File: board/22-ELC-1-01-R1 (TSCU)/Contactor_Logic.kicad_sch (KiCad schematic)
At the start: 16 parts, among them U2 74AUC1G17, U5 LM393, U6 74HC08_2AND

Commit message: Ready for review
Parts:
- removed R40, R44: 500, symbol Device:R
- removed unit 2 of U5
- renumbered C13 to C10, C11 to C8, C12 to C9, R23 to R15, R24 to R16, R25 to R19, TP5 to TP10, TP6 to TP11, TP18 to TP12, TP7 to TP13, U2 to U3, U5 to U4, U6 to U5

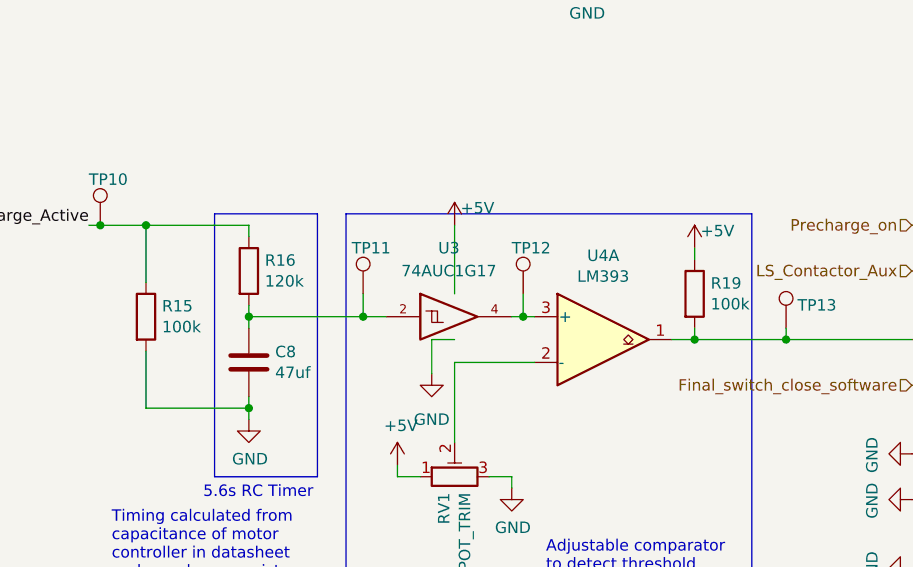
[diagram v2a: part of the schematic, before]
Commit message: All good except need to switch everything to accepting 24v power
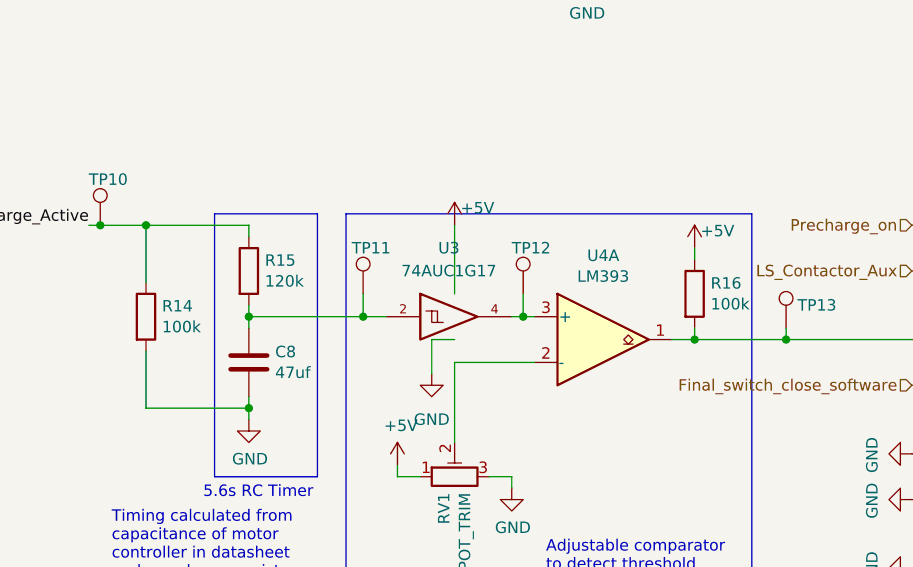
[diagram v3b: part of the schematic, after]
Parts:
- U3: footprint (none) -> Package_TO_SOT_SMD:SOT-23-5
- renumbered R15 to R14, R16 to R15, R19 to R16
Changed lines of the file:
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@@
   (symbol (lib_id "power:+5V") (at 119.38 130.81 0) (unit 1)
     (in_bom yes) (on_board yes)
-    (property "Reference" "#PWR038" (id 0) (at 119.38 134.62 0)
+    (property "Reference" "#PWR039" (id 0) (at 119.38 134.62 0)
       (effects (font (size 1.27 1.27)) hide)
     )
@@
   (symbol (lib_id "power:GND") (at 132.08 133.35 0) (unit 1)
     (in_bom yes) (on_board yes)
-    (property "Reference" "#PWR041" (id 0) (at 132.08 139.7 0)
+    (property "Reference" "#PWR042" (id 0) (at 132.08 139.7 0)
       (effects (font (size 1.27 1.27)) hide)
     )
@@
   (symbol (lib_id "Device:R") (at 102.87 109.22 0) (unit 1)
     (in_bom yes) (on_board yes)
-    (property "Reference" "R16" (id 0) (at 104.648 108.0516 0)
+    (property "Reference" "R15" (id 0) (at 104.648 108.0516 0)
       (effects (font (size 1.27 1.27)) (justify left))
     )
@@
   (symbol (lib_id "power:GND") (at 102.87 125.73 0) (unit 1)
     (in_bom yes) (on_board yes)
-    (property "Reference" "#PWR037" (id 0) (at 102.87 132.08 0)
+    (property "Reference" "#PWR038" (id 0) (at 102.87 132.08 0)
       (effects (font (size 1.27 1.27)) hide)
     )
@@
   (symbol (lib_id "Device:R") (at 91.44 114.3 0) (unit 1)
     (in_bom yes) (on_board yes)
-    (property "Reference" "R15" (id 0) (at 93.218 113.1316 0)
+    (property "Reference" "R14" (id 0) (at 93.218 113.1316 0)
       (effects (font (size 1.27 1.27)) (justify left))
     )
@@
   (symbol (lib_id "Device:R") (at 152.4 111.76 0) (unit 1)
     (in_bom yes) (on_board yes)
-    (property "Reference" "R19" (id 0) (at 154.178 110.5916 0)
+    (property "Reference" "R16" (id 0) (at 154.178 110.5916 0)
       (effects (font (size 1.27 1.27)) (justify left))
     )
@@
     (property "Reference" "U3" (id 0) (at 125.095 106.68 0))
     (property "Value" "74AUC1G17" (id 1) (at 125.095 109.22 0))
-    (property "Footprint" "" (id 2) (at 125.73 114.3 0)
+    (property "Footprint" "Package_TO_SOT_SMD:SOT-23-5" (id 2) (at 125.73 114.3 0)
       (effects (font (size 1.27 1.27)) hide)
     )
@@
   (symbol (lib_id "power:+5V") (at 125.73 104.14 0) (unit 1)
     (in_bom yes) (on_board yes)
-    (property "Reference" "#PWR040" (id 0) (at 125.73 107.95 0)
+    (property "Reference" "#PWR041" (id 0) (at 125.73 107.95 0)
       (effects (font (size 1.27 1.27)) hide)
     )
@@
   (symbol (lib_id "power:GND") (at 123.19 120.65 0) (unit 1)
     (in_bom yes) (on_board yes) (fields_autoplaced)
-    (property "Reference" "#PWR039" (id 0) (at 123.19 127 0)
-      (effects (font (size 1.27 1.27)) hide)
-    )
+    (property "Reference" "#PWR040" (id 0) (at 123.19 127 0)
+      (effects (font (size 1.27 1.27)) hide)
+    )

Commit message: Finalized schematic, started board layout
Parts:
- C10, C9: footprint Capacitor_SMD:C_0603_1608Metric_Pad1.08x0.95mm_HandSolder -> Capacitor_SMD:C_0402_1005Metric
- C8: footprint Capacitor_SMD:C_1206_3216Metric_Pad1.33x1.80mm_HandSolder -> Capacitor_SMD:C_0402_1005Metric
- R14, R15, R16: footprint Resistor_SMD:R_0603_1608Metric_Pad0.98x0.95mm_HandSolder -> FixedTextSizes:R_0402_1005Metric
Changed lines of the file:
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@@
   (symbol (lib_id "power:+5V") (at 119.38 130.81 0) (unit 1)
     (in_bom yes) (on_board yes)
-    (property "Reference" "#PWR039" (id 0) (at 119.38 134.62 0)
+    (property "Reference" "#PWR038" (id 0) (at 119.38 134.62 0)
       (effects (font (size 1.27 1.27)) hide)
     )
@@
   (symbol (lib_id "power:GND") (at 132.08 133.35 0) (unit 1)
     (in_bom yes) (on_board yes)
-    (property "Reference" "#PWR042" (id 0) (at 132.08 139.7 0)
+    (property "Reference" "#PWR041" (id 0) (at 132.08 139.7 0)
       (effects (font (size 1.27 1.27)) hide)
     )
@@
       (effects (font (size 1.27 1.27)) (justify left))
     )
-    (property "Footprint" "Resistor_SMD:R_0603_1608Metric_Pad0.98x0.95mm_HandSolder" (id 2) (at 101.092 109.22 90)
+    (property "Footprint" "FixedTextSizes:R_0402_1005Metric" (id 2) (at 101.092 109.22 90)
       (effects (font (size 1.27 1.27)) hide)
     )
@@
       (effects (font (size 1.27 1.27)) (justify left))
     )
-    (property "Footprint" "Capacitor_SMD:C_1206_3216Metric_Pad1.33x1.80mm_HandSolder" (id 2) (at 103.8352 123.19 0)
+    (property "Footprint" "Capacitor_SMD:C_0402_1005Metric" (id 2) (at 103.8352 123.19 0)
       (effects (font (size 1.27 1.27)) hide)
     )
@@
   (symbol (lib_id "power:GND") (at 102.87 125.73 0) (unit 1)
     (in_bom yes) (on_board yes)
-    (property "Reference" "#PWR038" (id 0) (at 102.87 132.08 0)
+    (property "Reference" "#PWR037" (id 0) (at 102.87 132.08 0)
       (effects (font (size 1.27 1.27)) hide)
     )
@@
       (effects (font (size 1.27 1.27)) (justify left))
     )
-    (property "Footprint" "Resistor_SMD:R_0603_1608Metric_Pad0.98x0.95mm_HandSolder" (id 2) (at 89.662 114.3 90)
+    (property "Footprint" "FixedTextSizes:R_0402_1005Metric" (id 2) (at 89.662 114.3 90)
       (effects (font (size 1.27 1.27)) hide)
     )
@@
   (symbol (lib_id "power:+5V") (at 187.96 83.82 0) (unit 1)
     (in_bom yes) (on_board yes)
-    (property "Reference" "#PWR051" (id 0) (at 187.96 87.63 0)
+    (property "Reference" "#PWR050" (id 0) (at 187.96 87.63 0)
       (effects (font (size 1.27 1.27)) hide)
     )
@@
     (property "Reference" "C10" (id 0) (at 193.04 81.8134 90))
     (property "Value" "0.1uf" (id 1) (at 193.04 84.1248 90))
-    (property "Footprint" "Capacitor_SMD:C_0603_1608Metric_Pad1.08x0.95mm_HandSolder" (id 2) (at 193.04 87.63 0)
+    (property "Footprint" "Capacitor_SMD:C_0402_1005Metric" (id 2) (at 193.04 87.63 0)
       (effects (font (size 1.27 1.27)) hide)
     )
@@
   (symbol (lib_id "power:GND") (at 187.96 151.13 0) (unit 1)
     (in_bom yes) (on_board yes)
-    (property "Reference" "#PWR052" (id 0) (at 187.96 157.48 0)
+    (property "Reference" "#PWR051" (id 0) (at 187.96 157.48 0)
       (effects (font (size 1.27 1.27)) hide)
     )
@@
   (symbol (lib_id "power:GND") (at 196.85 88.9 0) (unit 1)
     (in_bom yes) (on_board yes)
-    (property "Reference" "#PWR053" (id 0) (at 196.85 95.25 0)
+    (property "Reference" "#PWR052" (id 0) (at 196.85 95.25 0)
       (effects (font (size 1.27 1.27)) hide)
     )
@@
   (symbol (lib_id "power:+5V") (at 140.335 54.61 0) (unit 1)
     (in_bom yes) (on_board yes)
-    (property "Reference" "#PWR043" (id 0) (at 140.335 58.42 0)
+    (property "Reference" "#PWR042" (id 0) (at 140.335 58.42 0)
       (effects (font (size 1.27 1.27)) hide)
     )
@@
   (symbol (lib_id "power:GND") (at 140.335 76.2 0) (unit 1)
     (in_bom yes) (on_board yes)
-    (property "Reference" "#PWR044" (id 0) (at 140.335 82.55 0)
+    (property "Reference" "#PWR043" (id 0) (at 140.335 82.55 0)
       (effects (font (size 1.27 1.27)) hide)
     )
@@
     (property "Reference" "C9" (id 0) (at 146.685 51.3334 90))
     (property "Value" "0.1uf" (id 1) (at 146.685 53.6448 90))
-    (property "Footprint" "Capacitor_SMD:C_0603_1608Metric_Pad1.08x0.95mm_HandSolder" (id 2) (at 146.685 57.15 0)
+    (property "Footprint" "Capacitor_SMD:C_0402_1005Metric" (id 2) (at 146.685 57.15 0)
       (effects (font (size 1.27 1.27)) hide)
     )
@@
   (symbol (lib_id "power:GND") (at 150.495 58.42 0) (unit 1)
     (in_bom yes) (on_board yes)
-    (property "Reference" "#PWR045" (id 0) (at 150.495 64.77 0)
+    (property "Reference" "#PWR044" (id 0) (at 150.495 64.77 0)
       (effects (font (size 1.27 1.27)) hide)
     )
@@
       (effects (font (size 1.27 1.27)) (justify left))
     )
-    (property "Footprint" "Resistor_SMD:R_0603_1608Metric_Pad0.98x0.95mm_HandSolder" (id 2) (at 150.622 111.76 90)
+    (property "Footprint" "FixedTextSizes:R_0402_1005Metric" (id 2) (at 150.622 111.76 90)
       (effects (font (size 1.27 1.27)) hide)
     )
@@
   (symbol (lib_id "power:+5V") (at 152.4 106.68 0) (unit 1)
     (in_bom yes) (on_board yes)
-    (property "Reference" "#PWR046" (id 0) (at 152.4 110.49 0)
+    (property "Reference" "#PWR045" (id 0) (at 152.4 110.49 0)
       (effects (font (size 1.27 1.27)) hide)
     )
@@
   (symbol (lib_id "power:GND") (at 176.53 129.54 270) (unit 1)
     (in_bom yes) (on_board yes)
-    (property "Reference" "#PWR047" (id 0) (at 170.18 129.54 0)
+    (property "Reference" "#PWR046" (id 0) (at 170.18 129.54 0)
       (effects (font (size 1.27 1.27)) hide)
     )
@@
   (symbol (lib_id "power:GND") (at 176.53 134.62 270) (unit 1)
     (in_bom yes) (on_board yes)
-    (property "Reference" "#PWR048" (id 0) (at 170.18 134.62 0)
+    (property "Reference" "#PWR047" (id 0) (at 170.18 134.62 0)
       (effects (font (size 1.27 1.27)) hide)
     )
@@
   (symbol (lib_id "power:GND") (at 176.53 142.24 270) (unit 1)
     (in_bom yes) (on_board yes)
-    (property "Reference" "#PWR049" (id 0) (at 170.18 142.24 0)
+    (property "Reference" "#PWR048" (id 0) (at 170.18 142.24 0)
       (effects (font (size 1.27 1.27)) hide)
     )
@@
   (symbol (lib_id "power:GND") (at 176.53 147.32 270) (unit 1)
     (in_bom yes) (on_board yes)
-    (property "Reference" "#PWR050" (id 0) (at 170.18 147.32 0)
+    (property "Reference" "#PWR049" (id 0) (at 170.18 147.32 0)
       (effects (font (size 1.27 1.27)) hide)
     )
@@
   (symbol (lib_id "power:+5V") (at 125.73 104.14 0) (unit 1)
     (in_bom yes) (on_board yes)
-    (property "Reference" "#PWR041" (id 0) (at 125.73 107.95 0)
+    (property "Reference" "#PWR040" (id 0) (at 125.73 107.95 0)
       (effects (font (size 1.27 1.27)) hide)
     )
@@
   (symbol (lib_id "power:GND") (at 123.19 120.65 0) (unit 1)
     (in_bom yes) (on_board yes) (fields_autoplaced)
-    (property "Reference" "#PWR040" (id 0) (at 123.19 127 0)
-      (effects (font (size 1.27 1.27)) hide)
-    )
+    (property "Reference" "#PWR039" (id 0) (at 123.19 127 0)
+      (effects (font (size 1.27 1.27)) hide)
+    )

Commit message: More progress
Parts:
- C10, C8, C9: footprint Capacitor_SMD:C_0402_1005Metric -> FixedTextSizes:C_0402_1005Metric_Pad0.74x0.62mm_HandSolder_Reasonable_Text_Size
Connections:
- net Precharge_Timer_Out: now reaches C8.1, R15.2, TP11.1, U3.2
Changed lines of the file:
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@@
 (kicad_sch (version 20211123) (generator eeschema)
   (paper "A4")
+  (junction (at 111.76 114.3) (diameter 0) (color 0 0 0 0)
+  )
   (junction (at 152.4 116.84) (diameter 0) (color 0 0 0 0)
   )
@@
     (stroke (width 0) (type default) (color 0 0 0 0))
   )
-  (wire (pts (xy 102.87 114.3) (xy 115.57 114.3))
+  (wire (pts (xy 102.87 114.3) (xy 111.76 114.3))
     (stroke (width 0) (type default) (color 0 0 0 0))
   )
@@
     (stroke (width 0) (type default) (color 0 0 0 0))
   )
+  (wire (pts (xy 113.03 96.52) (xy 111.76 96.52))
+    (stroke (width 0) (type default) (color 0 0 0 0))
+  )
   (wire (pts (xy 133.35 111.76) (xy 133.35 114.3))
     (stroke (width 0) (type default) (color 0 0 0 0))
@@
     (stroke (width 0) (type default) (color 0 0 0 0))
   )
+  (wire (pts (xy 111.76 114.3) (xy 115.57 114.3))
+    (stroke (width 0) (type default) (color 0 0 0 0))
+  )
   (polyline (pts (xy 99.06 132.08) (xy 99.06 102.87))
     (stroke (width 0) (type default) (color 0 0 0 0))
@@
   )
   (wire (pts (xy 115.57 111.76) (xy 115.57 114.3))
+    (stroke (width 0) (type default) (color 0 0 0 0))
+  )
+  (wire (pts (xy 111.76 96.52) (xy 111.76 114.3))
     (stroke (width 0) (type default) (color 0 0 0 0))
   )
@@
     (effects (font (size 1.27 1.27)) (justify right))
   )
+  (hierarchical_label "Precharge_Timer_Out" (shape output) (at 113.03 96.52 0)
+    (effects (font (size 1.27 1.27)) (justify left))
+  )
   (hierarchical_label "Precharge_done" (shape output) (at 205.74 119.38 0)
     (effects (font (size 1.27 1.27)) (justify left))
@@
   (symbol (lib_id "power:+5V") (at 119.38 130.81 0) (unit 1)
     (in_bom yes) (on_board yes)
-    (property "Reference" "#PWR038" (id 0) (at 119.38 134.62 0)
+    (property "Reference" "#PWR041" (id 0) (at 119.38 134.62 0)
       (effects (font (size 1.27 1.27)) hide)
     )
@@
   (symbol (lib_id "power:GND") (at 132.08 133.35 0) (unit 1)
     (in_bom yes) (on_board yes)
-    (property "Reference" "#PWR041" (id 0) (at 132.08 139.7 0)
+    (property "Reference" "#PWR044" (id 0) (at 132.08 139.7 0)
       (effects (font (size 1.27 1.27)) hide)
     )
@@
       (effects (font (size 1.27 1.27)) (justify left))
     )
-    (property "Footprint" "Capacitor_SMD:C_0402_1005Metric" (id 2) (at 103.8352 123.19 0)
+    (property "Footprint" "FixedTextSizes:C_0402_1005Metric_Pad0.74x0.62mm_HandSolder_Reasonable_Text_Size" (id 2) (at 103.8352 123.19 0)
       (effects (font (size 1.27 1.27)) hide)
     )
@@
   (symbol (lib_id "power:GND") (at 102.87 125.73 0) (unit 1)
     (in_bom yes) (on_board yes)
-    (property "Reference" "#PWR037" (id 0) (at 102.87 132.08 0)
+    (property "Reference" "#PWR040" (id 0) (at 102.87 132.08 0)
       (effects (font (size 1.27 1.27)) hide)
     )
@@
   (symbol (lib_id "power:+5V") (at 187.96 83.82 0) (unit 1)
     (in_bom yes) (on_board yes)
-    (property "Reference" "#PWR050" (id 0) (at 187.96 87.63 0)
+    (property "Reference" "#PWR053" (id 0) (at 187.96 87.63 0)
       (effects (font (size 1.27 1.27)) hide)
     )
@@
     (property "Reference" "C10" (id 0) (at 193.04 81.8134 90))
     (property "Value" "0.1uf" (id 1) (at 193.04 84.1248 90))
-    (property "Footprint" "Capacitor_SMD:C_0402_1005Metric" (id 2) (at 193.04 87.63 0)
+    (property "Footprint" "FixedTextSizes:C_0402_1005Metric_Pad0.74x0.62mm_HandSolder_Reasonable_Text_Size" (id 2) (at 193.04 87.63 0)
       (effects (font (size 1.27 1.27)) hide)
     )
@@
   (symbol (lib_id "power:GND") (at 187.96 151.13 0) (unit 1)
     (in_bom yes) (on_board yes)
-    (property "Reference" "#PWR051" (id 0) (at 187.96 157.48 0)
+    (property "Reference" "#PWR054" (id 0) (at 187.96 157.48 0)
       (effects (font (size 1.27 1.27)) hide)
     )
@@
   (symbol (lib_id "power:GND") (at 196.85 88.9 0) (unit 1)
     (in_bom yes) (on_board yes)
-    (property "Reference" "#PWR052" (id 0) (at 196.85 95.25 0)
+    (property "Reference" "#PWR055" (id 0) (at 196.85 95.25 0)
       (effects (font (size 1.27 1.27)) hide)
     )
@@
   (symbol (lib_id "power:+5V") (at 140.335 54.61 0) (unit 1)
     (in_bom yes) (on_board yes)
-    (property "Reference" "#PWR042" (id 0) (at 140.335 58.42 0)
+    (property "Reference" "#PWR045" (id 0) (at 140.335 58.42 0)
       (effects (font (size 1.27 1.27)) hide)
     )
@@
   (symbol (lib_id "power:GND") (at 140.335 76.2 0) (unit 1)
     (in_bom yes) (on_board yes)
-    (property "Reference" "#PWR043" (id 0) (at 140.335 82.55 0)
+    (property "Reference" "#PWR046" (id 0) (at 140.335 82.55 0)
       (effects (font (size 1.27 1.27)) hide)
     )
@@
     (property "Reference" "C9" (id 0) (at 146.685 51.3334 90))
     (property "Value" "0.1uf" (id 1) (at 146.685 53.6448 90))
-    (property "Footprint" "Capacitor_SMD:C_0402_1005Metric" (id 2) (at 146.685 57.15 0)
+    (property "Footprint" "FixedTextSizes:C_0402_1005Metric_Pad0.74x0.62mm_HandSolder_Reasonable_Text_Size" (id 2) (at 146.685 57.15 0)
       (effects (font (size 1.27 1.27)) hide)
     )
@@
   (symbol (lib_id "power:GND") (at 150.495 58.42 0) (unit 1)
     (in_bom yes) (on_board yes)
-    (property "Reference" "#PWR044" (id 0) (at 150.495 64.77 0)
+    (property "Reference" "#PWR047" (id 0) (at 150.495 64.77 0)
       (effects (font (size 1.27 1.27)) hide)
     )
@@
   (symbol (lib_id "power:+5V") (at 152.4 106.68 0) (unit 1)
     (in_bom yes) (on_board yes)
-    (property "Reference" "#PWR045" (id 0) (at 152.4 110.49 0)
+    (property "Reference" "#PWR048" (id 0) (at 152.4 110.49 0)
       (effects (font (size 1.27 1.27)) hide)
     )
@@
   (symbol (lib_id "power:GND") (at 176.53 129.54 270) (unit 1)
     (in_bom yes) (on_board yes)
-    (property "Reference" "#PWR046" (id 0) (at 170.18 129.54 0)
+    (property "Reference" "#PWR049" (id 0) (at 170.18 129.54 0)
       (effects (font (size 1.27 1.27)) hide)
     )
@@
   (symbol (lib_id "power:GND") (at 176.53 134.62 270) (unit 1)
     (in_bom yes) (on_board yes)
-    (property "Reference" "#PWR047" (id 0) (at 170.18 134.62 0)
+    (property "Reference" "#PWR050" (id 0) (at 170.18 134.62 0)
       (effects (font (size 1.27 1.27)) hide)
     )
@@
   (symbol (lib_id "power:GND") (at 176.53 142.24 270) (unit 1)
     (in_bom yes) (on_board yes)
-    (property "Reference" "#PWR048" (id 0) (at 170.18 142.24 0)
+    (property "Reference" "#PWR051" (id 0) (at 170.18 142.24 0)
       (effects (font (size 1.27 1.27)) hide)
     )
@@
   (symbol (lib_id "power:GND") (at 176.53 147.32 270) (unit 1)
     (in_bom yes) (on_board yes)
-    (property "Reference" "#PWR049" (id 0) (at 170.18 147.32 0)
+    (property "Reference" "#PWR052" (id 0) (at 170.18 147.32 0)
       (effects (font (size 1.27 1.27)) hide)
     )
@@
   (symbol (lib_id "power:+5V") (at 125.73 104.14 0) (unit 1)
     (in_bom yes) (on_board yes)
-    (property "Reference" "#PWR040" (id 0) (at 125.73 107.95 0)
+    (property "Reference" "#PWR043" (id 0) (at 125.73 107.95 0)
       (effects (font (size 1.27 1.27)) hide)
     )
@@
   (symbol (lib_id "power:GND") (at 123.19 120.65 0) (unit 1)
     (in_bom yes) (on_board yes) (fields_autoplaced)
-    (property "Reference" "#PWR039" (id 0) (at 123.19 127 0)
-      (effects (font (size 1.27 1.27)) hide)
-    )
+    (property "Reference" "#PWR042" (id 0) (at 123.19 127 0)
+      (effects (font (size 1.27 1.27)) hide)
+    )
